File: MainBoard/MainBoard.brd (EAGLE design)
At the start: 99.2 x 83.5 mm, 47 parts, among them IC1 3.3V, P1 DF11-06-2DS, Q1 BC337-40, Q2 BSS138, Q3 BSS138, Q4 BS170, Q5 BS170

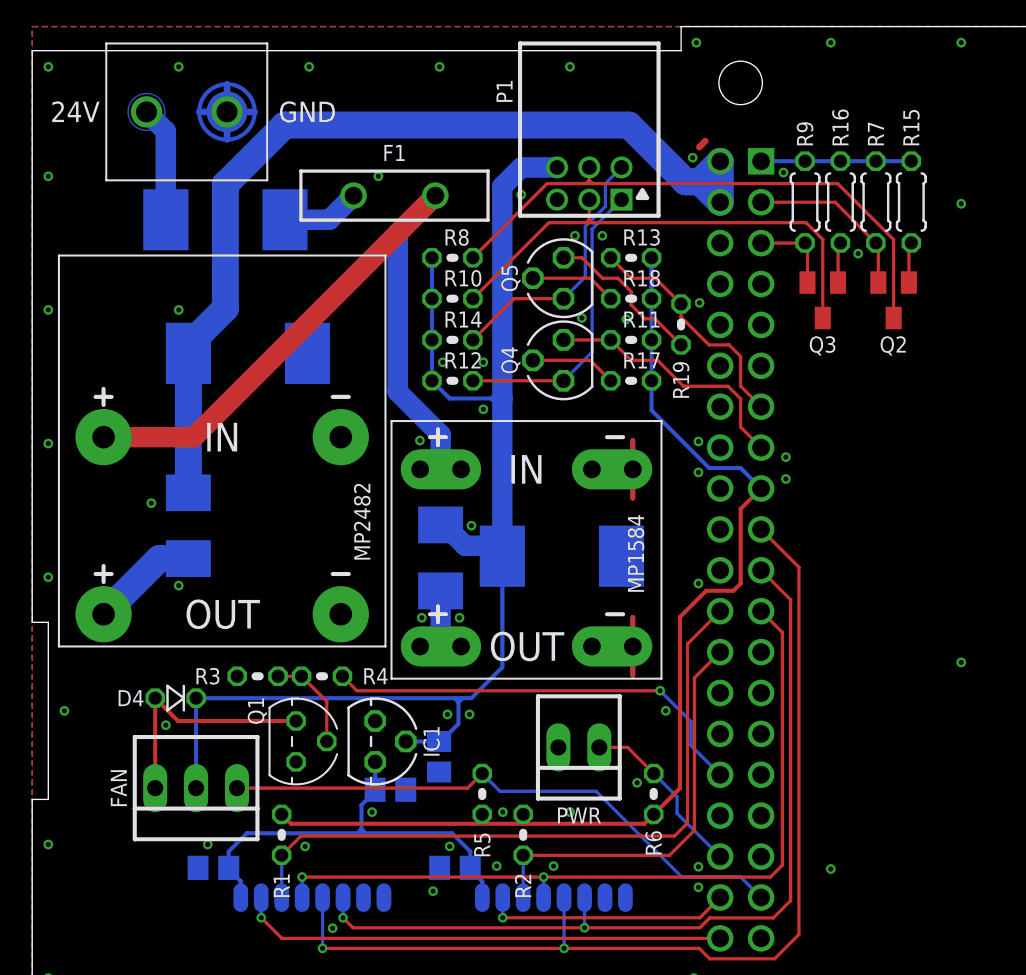
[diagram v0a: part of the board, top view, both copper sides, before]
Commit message: Replace On/Off fan with PWM driven one
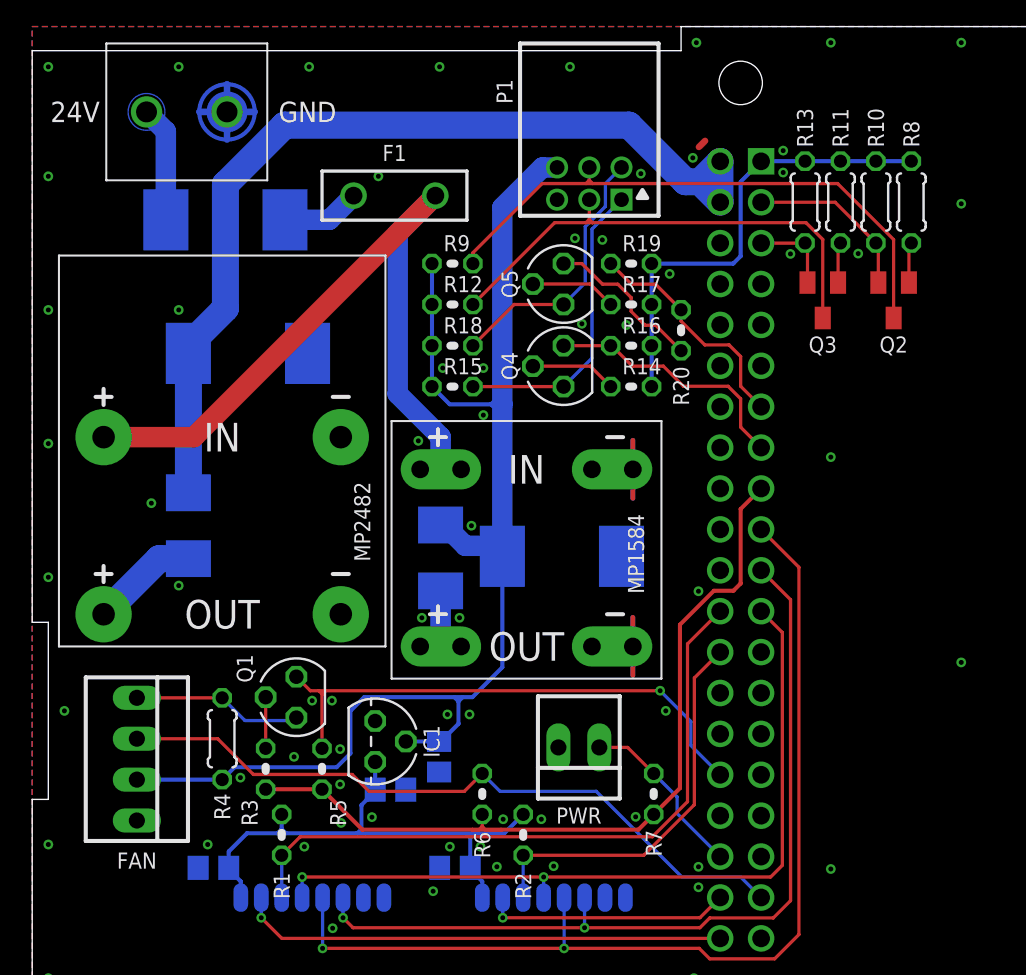
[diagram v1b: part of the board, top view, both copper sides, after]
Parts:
- removed D4: 1N4148, diode:DO35-2V
- added R20: 680R, rcl:0204V
- F1: value 1.5A -> 1.35A; device ptc:PTH_11MM -> ptc:RGEF250
- FAN: value 22-23-2031 -> 22-23-2041; device con-molex:22-23-2031 -> con-molex:22-23-2041
- Q1: value BC337-40 -> BS170; device transistor-npn:TO92 -> transistor-small-signal:SOT54E
- R10, R4: device rcl:0204V -> rcl:0204/5
- R11: value 10K -> 100R; device rcl:0204V -> rcl:0204/5
- R12: value 10K -> 1K
- R13: value 10K -> 1K; device rcl:0204V -> rcl:0204/5
- R14: value 10K -> 200R
- R15, R16: value 100R -> 1K8; device rcl:0204/5 -> rcl:0204V
- R17: value 100R -> 200R
- R18: value 100R -> 10K
- R19: value 680R -> 10K
- R3: value 10K -> 150R
- R5: value 10K -> 1K8
- R6: value 10K -> 1K2
- R7: value 1K -> 10K; device rcl:0204/5 -> rcl:0204V
- R8: value 1K -> 100R; device rcl:0204V -> rcl:0204/5
- R9: device rcl:0204/5 -> rcl:0204V
- moved R7 39.3 mm to (38.6, 35.8)
- moved R15 30.7 mm to (26.1, 61.1), turned to 0 degrees
- moved R8 28.7 mm to (54.6, 72.6), turned to 90 degrees
- moved R10 27.0 mm to (52.4, 72.6), turned to 90 degrees
- moved R9 22.2 mm to (26.1, 68.8), turned to 0 degrees
- moved R16 15.8 mm to (37.2, 63.7), turned to 0 degrees
- moved R11 15.6 mm to (50.2, 72.6), turned to 90 degrees
- moved R18 11.5 mm to (26.1, 63.7)
- moved R14 11.5 mm to (37.2, 61.1)
- moved R13 11.3 mm to (48.0, 72.6), turned to 90 degrees
- moved R6 10.7 mm to (27.9, 35.8)
- moved R5 10.1 mm to (18.0, 37.4), turned to 270 degrees
- moved R4 7.31 mm to (11.8, 39.3), turned to 90 degrees
- moved R3 5.77 mm to (14.5, 37.4), turned to 270 degrees
- moved R19 4.89 mm to (37.2, 68.8), turned to 0 degrees
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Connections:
- removed net 3V3: R1.2, R11.2, R13.2, R15.2, R16.2, R17.2, R18.2, R2.2, R5.1, R6.1, R7.2, R9.2, RPI.1, RPI.17
- removed net N$11: Q1.2, R3.2, R4.2
- removed net N$14: D4.A, FAN.3, Q1.3
- new net N$2: Q1.G, R3.1
- new net N$29: FAN.1, Q1.D, R4.2
- new net VCC: 433MHZ.VCC, 868MHZ.VCC, C1.1, C2.1, C3.1, IC1.3, R1.2, R2.2
- net +3V3: now also R10.2, R11.2, R13.2, R14.2, R16.2, R17.2, R19.2, R3.2, R5.2, R6.1, R7.1, R8.2, RPI.1, RPI.17; no longer 433MHZ.VCC, 868MHZ.VCC, C1.1, C2.1, C3.1, IC1.3
- net +5V: now also FAN.3, R15.1, R18.1, R4.1, R9.1; no longer D4.C, FAN.2, R10.1, R14.1, R8.1
- net GND: now also FAN.4; no longer Q1.1, R3.1
- net INT: now also R16.1; no longer R11.1
- net N$1: now also R12.2; no longer R10.2
- net N$12: now also R9.2; no longer R8.2
- net N$13: now also Q1.S, R5.1; no longer R4.1
- net N$21: now also R7.2; no longer R6.2
- net N$22: now also FAN.2, R6.2; no longer FAN.1, R5.2
- net N$23: now also R8.1; no longer R15.1
- net N$24: now also R11.1; no longer R16.1
- net N$25: now also R15.2; no longer R12.2
- net N$26: now also R18.2; no longer R14.2
- net N$27: now also R17.1; no longer R18.1
- net N$28: now also R14.1; no longer R17.1
- net N$5: now also R20.2; no longer R19.2
- net RESET: now also R20.1; no longer R13.1
- net SCL: now also R13.1; no longer R9.1
- net SDA: now also R10.1; no longer R7.1
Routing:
- net 3V3: track 78.9 -> 0.00 mm
- net +3V3: track 27.5 -> 81.1 mm
- net VCC: track 0.00 -> 34.1 mm
- net N$14: track 14.9 -> 0.00 mm
- net N$29: track 0.00 -> 10.6 mm
- net N$22: track 36.1 -> 43.8 mm
- net N$13: track 26.9 -> 33.7 mm
- net N$11: track 6.16 -> 0.00 mm
- net N$2: track 0.00 -> 3.18 mm
- net +5V: track 83.5 -> 84.8 mm
- net N$15: track 25.6 -> 24.7 mm
- net N$3: track 42.7 -> 41.9 mm
- net N$12: track 35.7 -> 36.3 mm
- net GND: vias 101 -> 107

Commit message: Fix DC/DC module footprint.
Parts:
- moved MP1584 0.40 mm to (31.1, 54.0)
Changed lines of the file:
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@@
 <attribute name="NAME" x="23.366" y="50.5" size="1" layer="26" font="vector" ratio="10" rot="MR90" align="top-center"/>
 </element>
-<element name="MP1584" library="modules" package="MP1584V" value="DC-DC-STEP-DOWN" x="30.7" y="54" smashed="yes" rot="R270">
-<attribute name="NAME" x="37" y="50.75" size="1" layer="25" font="vector" ratio="10" rot="R270" align="bottom-center"/>
-<attribute name="VALUE" x="19.27" y="54" size="1.27" layer="27" rot="R270" align="top-center"/>
+<element name="MP1584" library="modules" package="MP1584V" value="DC-DC-STEP-DOWN" x="31.096" y="54" smashed="yes" rot="R270">
+<attribute name="NAME" x="37.396" y="50.75" size="1" layer="25" font="vector" ratio="10" rot="R270" align="bottom-center"/>
+<attribute name="VALUE" x="19.666" y="54" size="1.27" layer="27" rot="R270" align="top-center"/>
 </element>
 <element name="MP2482" library="modules" package="MP2482V" value="DC-DC-STEP-DOWN" x="11.8" y="56" smashed="yes" rot="R270">
@@
 <contactref element="C1" pad="2"/>
 <contactref element="24V" pad="2"/>
-<wire x1="37.304" y1="57.8" x2="37.304" y2="54.2" width="0.3048" layer="16"/>
-<wire x1="37.304" y1="57.8" x2="37.304" y2="54.2" width="0.3048" layer="1"/>
+<wire x1="38.096" y1="57.8" x2="38.096" y2="54.2" width="0.3048" layer="16"/>
+<wire x1="38.096" y1="57.8" x2="38.096" y2="54.2" width="0.3048" layer="1"/>
 <contactref element="433MHZ" pad="GND0" route="any" routetag="G$1.GND"/>
 <contactref element="433MHZ" pad="GND1" route="any" routetag="G$1.GND"/>
@@
 <via x="41.03" y="75.345" extent="1-16" drill="0.3048" shape="octagon"/>
 <via x="37.8" y="74.365" extent="1-16" drill="0.3048" shape="octagon"/>
-<wire x1="37.304" y1="43.2" x2="37.304" y2="46.8" width="0.3048" layer="1"/>
-<wire x1="37.304" y1="43.2" x2="37.304" y2="46.8" width="0.3048" layer="16"/>
+<wire x1="38.096" y1="43.2" x2="38.096" y2="46.8" width="0.3048" layer="1"/>
+<wire x1="38.096" y1="43.2" x2="38.096" y2="46.8" width="0.3048" layer="16"/>
 <via x="23.98" y="57.77" extent="1-16" drill="0.3048" shape="octagon"/>
 <via x="27.28" y="52.5" extent="1-16" drill="0.3048" shape="octagon"/>
